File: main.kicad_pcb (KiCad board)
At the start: 4 copper layers, 125 x 101.6 mm, 181 parts, among them J1 SMA, J2 SMA, J3 CONN_01X01, J4 CONN_01X01, J5 CONN_01X01, J6 CONN_01X01, P1 SMA, P2 SMA, P3 SMA, Q1 THAT300, Q2 THAT300, Q3 THAT300, Q4 THAT300, U1 LT1994, U2 LT1994, U3 LT6232, U4 LT1365, U5 LT1994, U6 LT1994, U7 LT1994

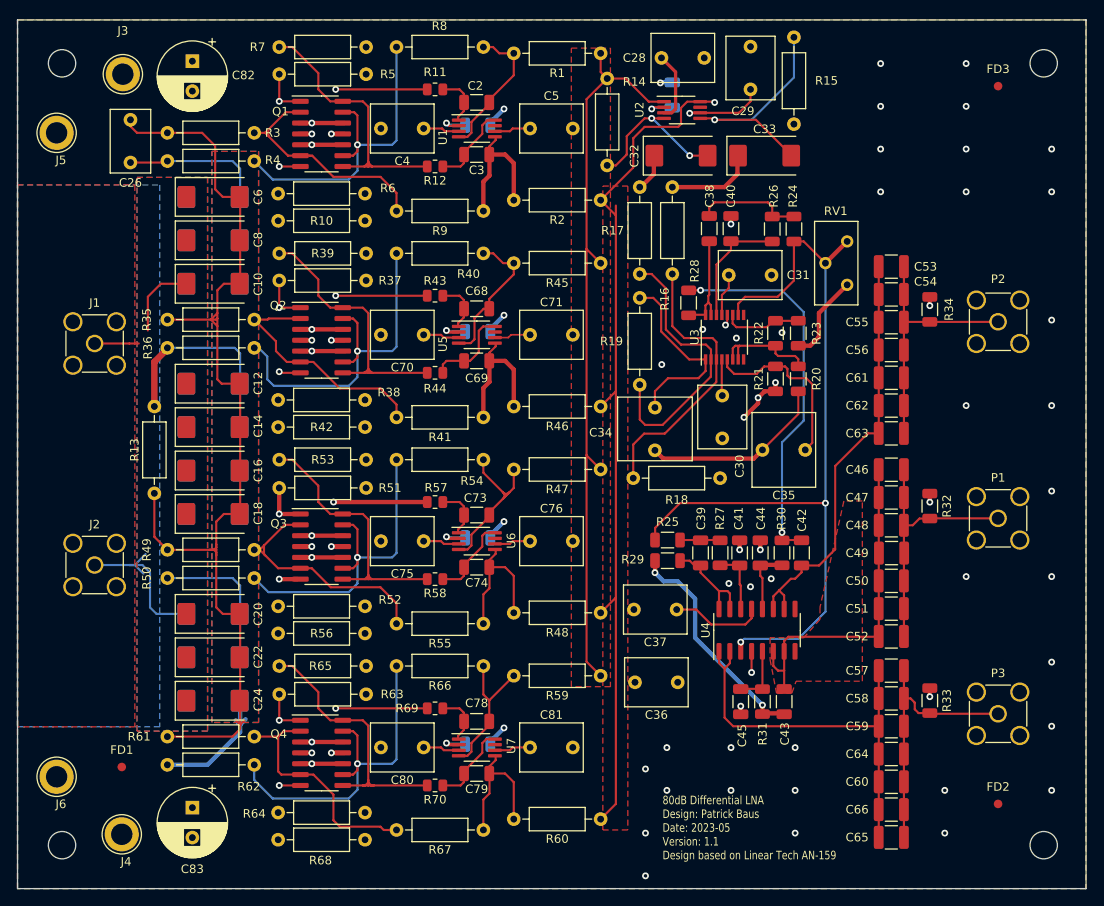
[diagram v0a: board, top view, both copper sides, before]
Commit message: Added silkscreen labels to input and outputs
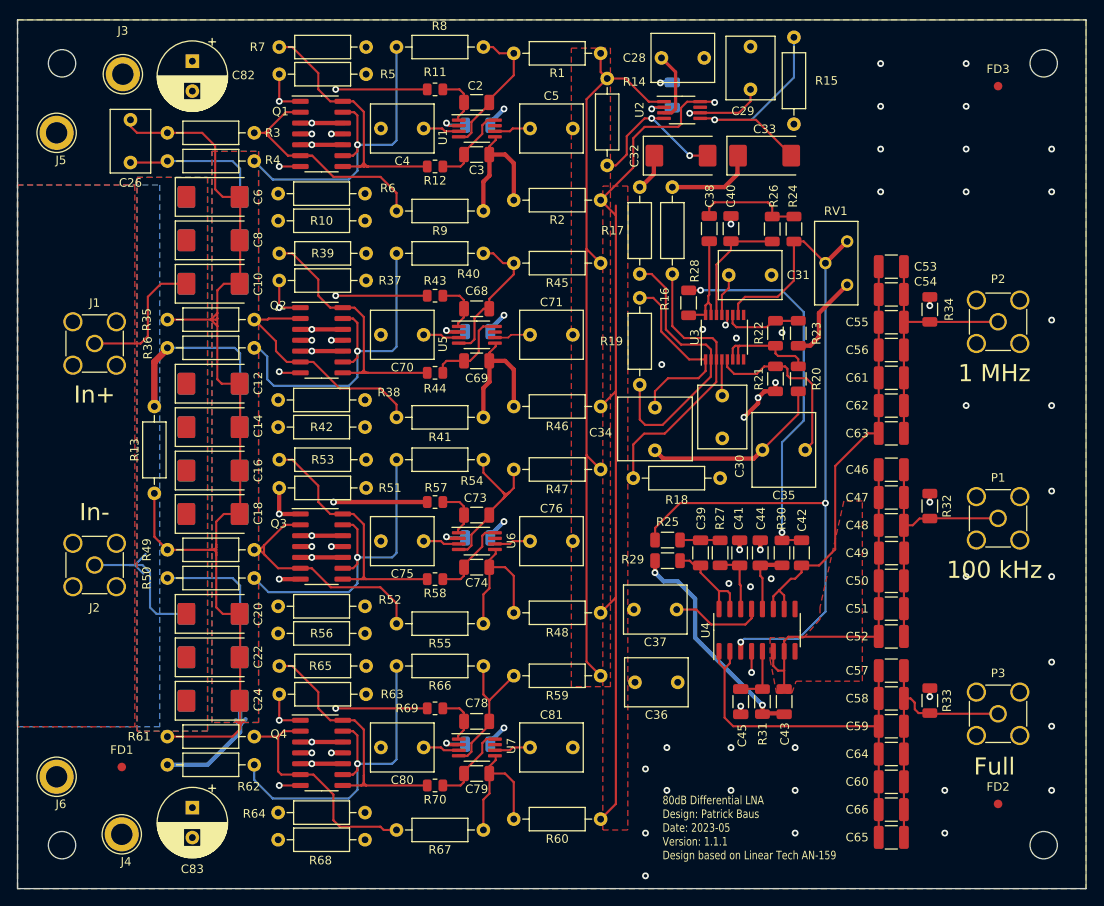
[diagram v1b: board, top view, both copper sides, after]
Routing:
- net /Input Filter/In+: track 14.2 -> 16.3 mm
- net Net-(Q3B-C): track 32.2 -> 31.1 mm
- net Net-(Q4B-C): track 32.9 -> 32.1 mm
- net Net-(Q1B-C): track 32.4 -> 31.7 mm
- net Net-(Q2B-C): track 32.3 -> 31.7 mm
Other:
- board text added: "1 MHz"
- board text added: "100 kHz"
- board text added: "80dB Differential LNA Design: Patrick Baus Date: 2023-05 Version: 1.1.1 Design based on Linear Tech AN-159"
- board text added: "Full"
- board text added: "In+"
- board text added: "In-"
- board text removed: "80dB Differential LNA Design: Patrick Baus Date: 2023-05 Version: 1.1 Design based on Linear Tech AN-159"
